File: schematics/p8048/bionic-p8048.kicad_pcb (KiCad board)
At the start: 2 copper layers, 27.9 x 68.6 mm, 9 parts, among them J1 Bionic-P135, J2 Bionic-P245, U1 P8048AH, U2 11AA010-I/TT

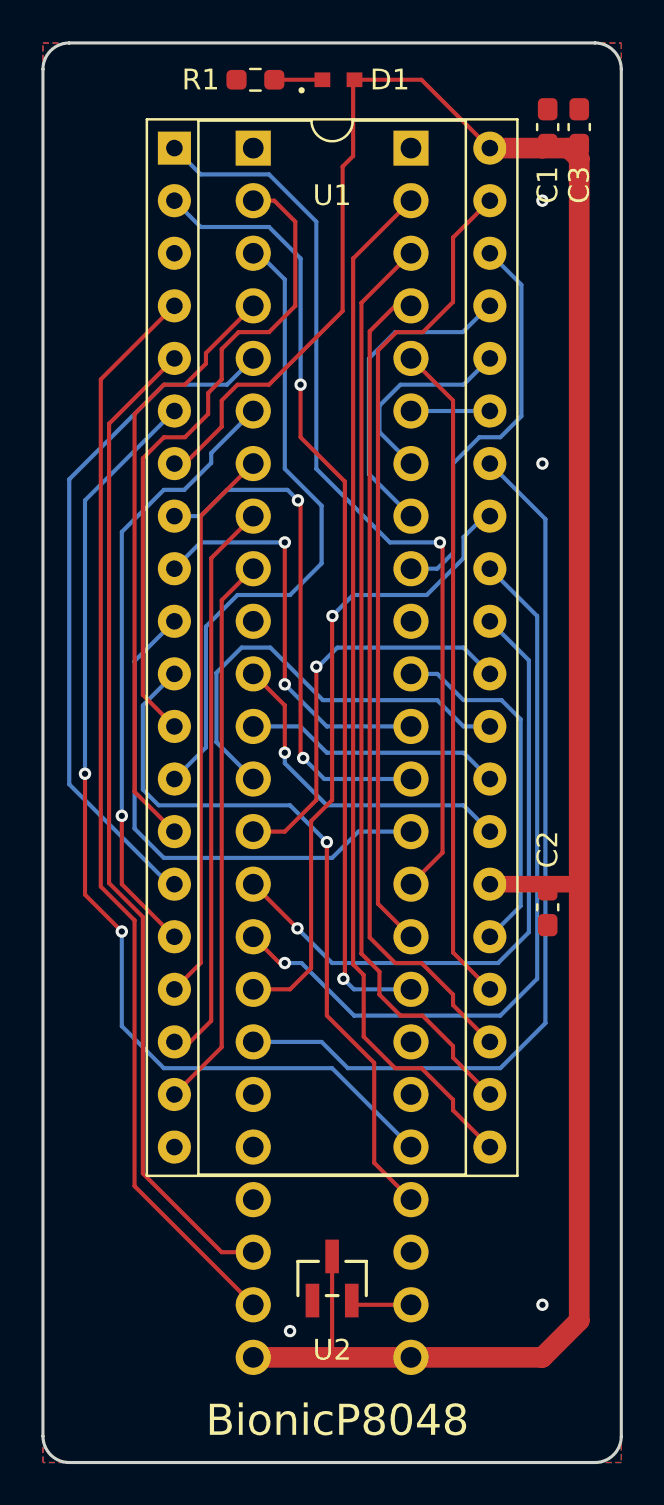
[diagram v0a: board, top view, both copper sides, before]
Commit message: [P8048] Fix EEPROM pinout
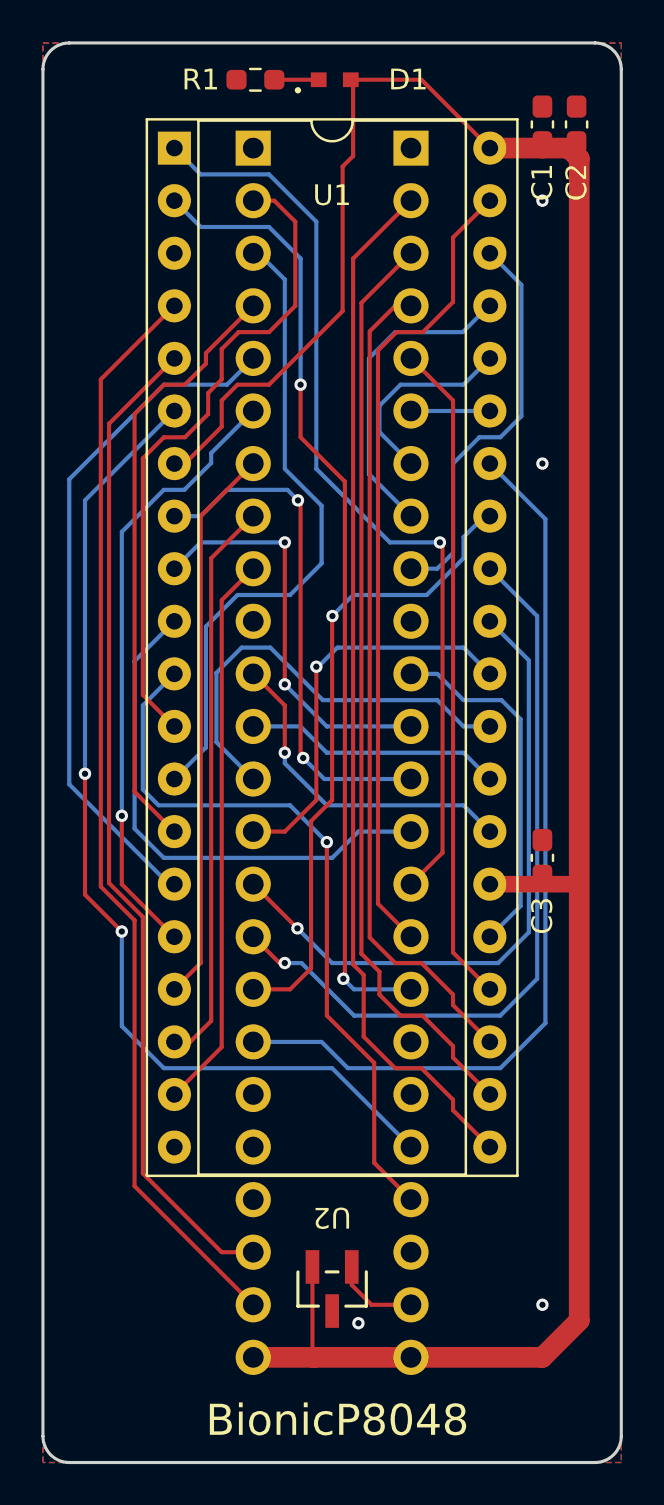
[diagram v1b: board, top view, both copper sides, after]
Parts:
- C2: renamed from C1; value 0.1u -> 22u
- C3: value 22u -> 0.1u
- moved C1 37.8 mm to (125.1, 73.9), turned to 90 degrees
- moved C3 35.4 mm to (125.1, 109.4)
- moved C2 1.40 mm to (126.8, 73.9)
- moved U2 0.51 mm to (115.0, 130.2), turned to 180 degrees
- moved D1 0.18 mm to (115.1, 71.8)
- renumbered C2 to C1
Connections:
- U2 pad 1: GND -> Net-(J2-P57)
- U2 pad 2: Net-(J2-P57) -> VCC
- U2 pad 3: VCC -> GND
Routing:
- net Net-(J2-P57): track 2.94 -> 4.13 mm
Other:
- board text added: "Rev. 5"
- board text removed: "Rev. 4"

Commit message: [P8048] Shrink board size
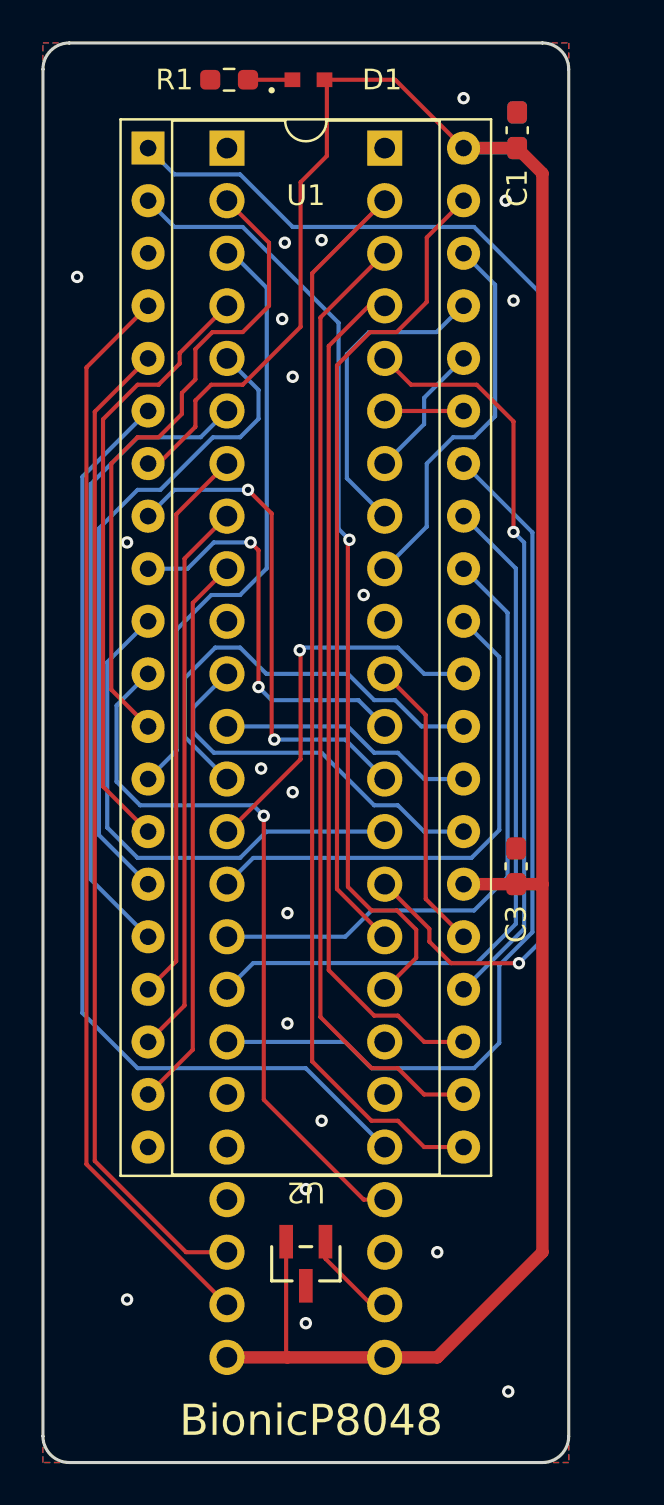
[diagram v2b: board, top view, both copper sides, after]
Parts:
- C2: moved to B.Cu
- moved C2 2.88 mm to (123.9, 74.2)
- moved U2 1.76 mm to (113.7, 129.0)
- moved C3 1.33 mm to (123.9, 109.8)
- moved D1 1.27 mm to (113.8, 71.8)
- moved J1 1.27 mm to (109.9, 75.1)
- moved J2 1.27 mm to (117.5, 75.1)
- moved R1 1.27 mm to (110.0, 71.8)
- moved U1 1.27 mm to (106.1, 75.1)
- moved C1 1.25 mm to (123.9, 74.2)
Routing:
- net /P44: track 44.9 -> 63.1 mm
- net /P34: track 31.3 -> 25.0 mm, vias 1 -> 0
- net /P35: track 36.8 -> 30.5 mm, vias 1 -> 0
- net /P36: track 30.9 -> 36.0 mm, vias 1 -> 0
- net /P23: track 32.1 -> 36.3 mm, vias 0 -> 1
- net /P40: track 17.3 -> 14.3 mm
- net /P25: track 9.71 -> 6.66 mm
- net /P30: track 16.2 -> 18.5 mm, vias 1 -> 0
- net /P21: track 44.8 -> 46.7 mm
- net /P11: track 31.4 -> 29.5 mm
- net /P20: track 50.4 -> 52.1 mm
- net /P22: track 40.0 -> 41.6 mm
- net /P13: track 33.1 -> 31.6 mm
- net /P14: track 29.7 -> 31.1 mm, vias 1 -> 0
- net /P54: track 48.6 -> 47.7 mm, vias 2 -> 0
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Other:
- board size 27.9 x 68.6 mm -> 25.4 x 68.6 mm

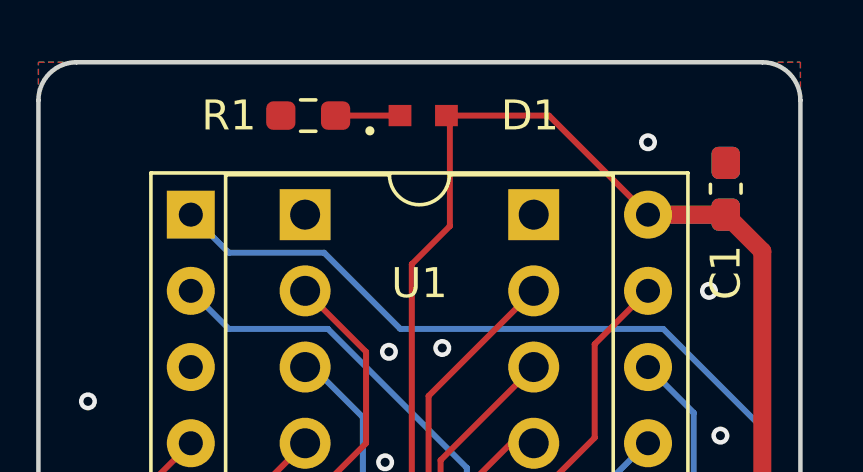
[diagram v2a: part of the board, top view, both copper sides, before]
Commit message: [schematics] Update LED footprint
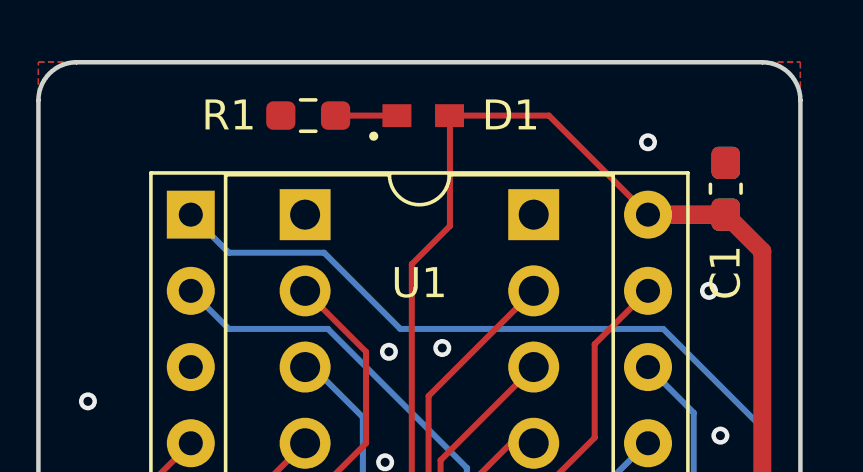
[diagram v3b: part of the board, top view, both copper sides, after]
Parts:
- D1: footprint 0-LocalLibrary:LED_CSL1901UW1_ROM -> 0-LocalLibrary:LED_CSL1901UW1_ROM-M

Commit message: [P8048] Cleanup schematics
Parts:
- D1: footprint 0-LocalLibrary:LED_CSL1901UW1_ROM-M -> rhom:LED_CSL1901UW1_ROM-M
- J1: footprint 0-LocalLibrary:Bionic-P135_Vertical -> bionic:Bionic-P135_Vertical
- J2: footprint 0-LocalLibrary:Bionic-P245_Vertical -> bionic:Bionic-P245_Vertical
- U1: footprint 0-LocalLibrary:DIP-40_W15.24mm_Socket -> bionic:DIP-40_W15.24mm_Socket
- U2: footprint 0-LocalLibrary:SOT-23_MC_MCH-M -> microchip:SOT-23_MC_MCH-M
- moved U2 0.41 mm to (113.7, 129.4)
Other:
- rule pad_to_mask_clearance: 0.051 -> 0

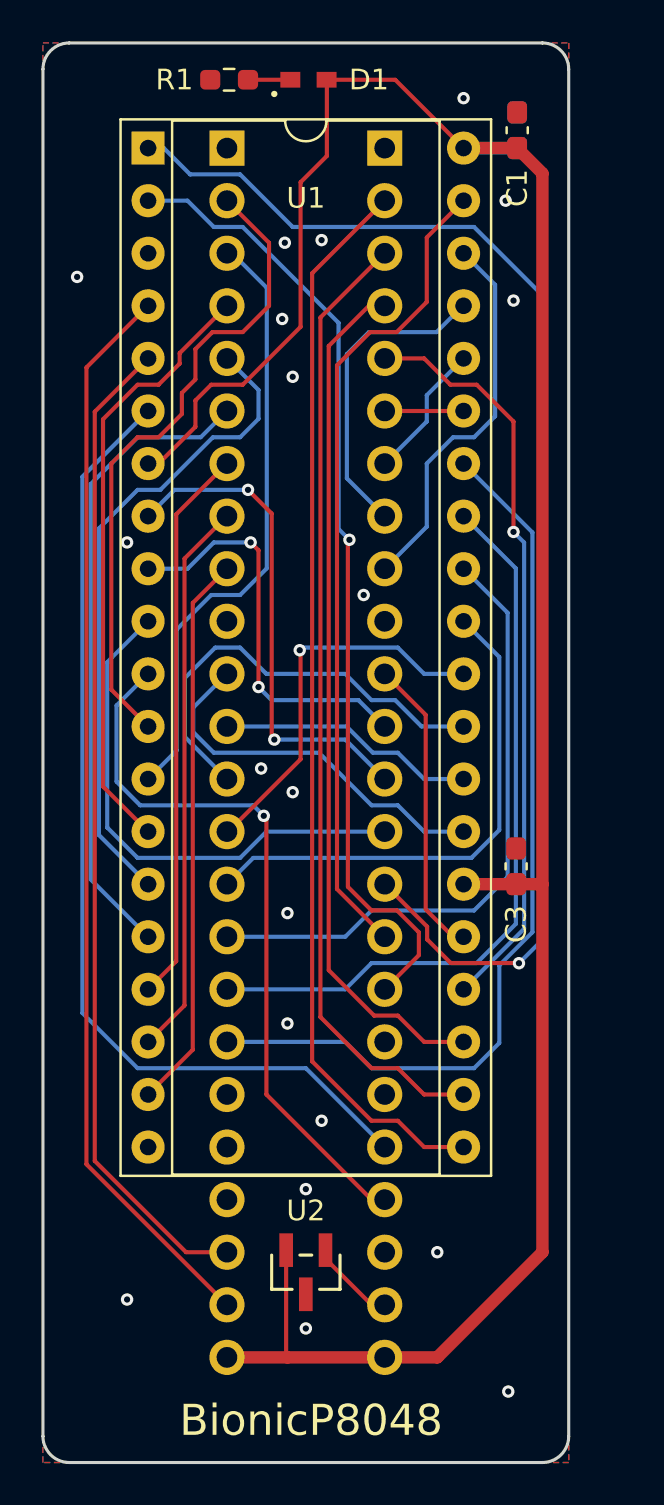
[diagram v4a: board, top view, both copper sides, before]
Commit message: [P8048] Update schematics
Remove unused pins from bionic connector
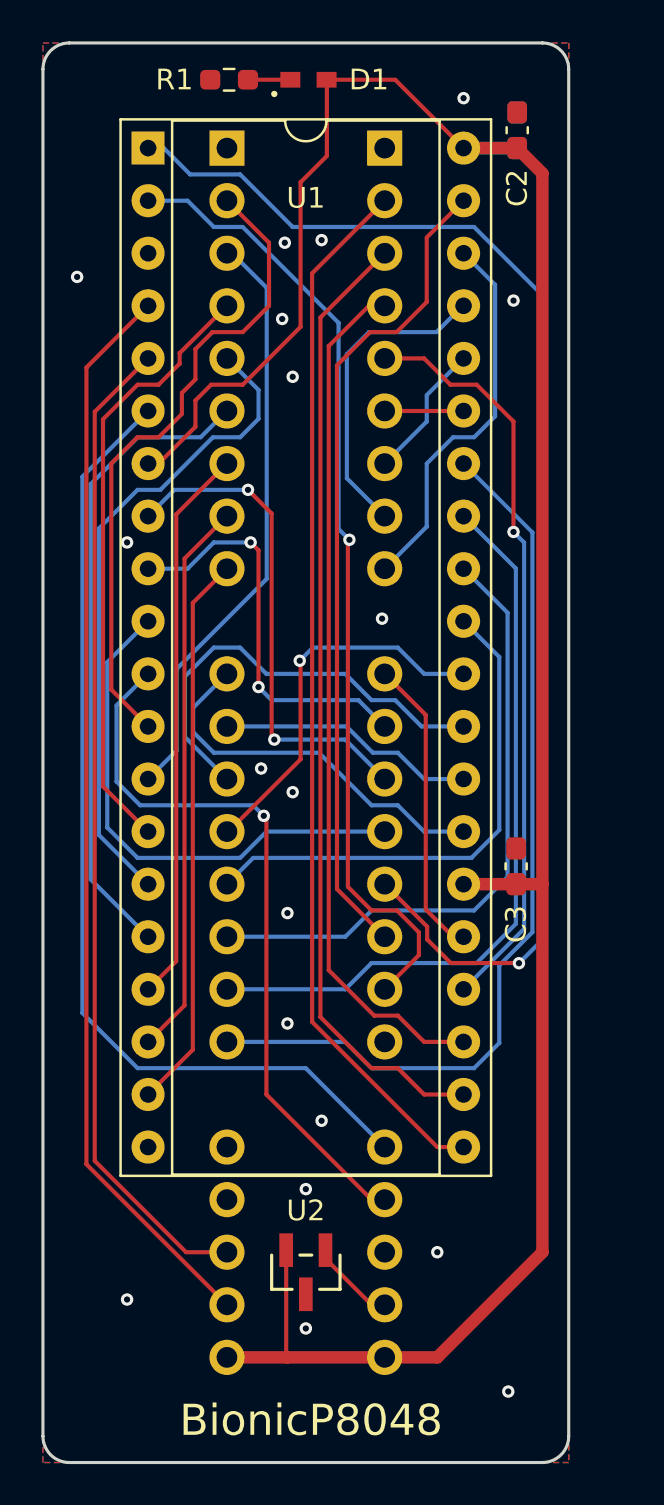
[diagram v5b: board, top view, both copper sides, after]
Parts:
- C1: moved to B.Cu
- C2: moved to F.Cu
- J1: footprint bionic:Bionic-P135_Vertical -> bionic:Bionic-P135_THT
- J2: footprint bionic:Bionic-P245_Vertical -> bionic:Bionic-P245_THT
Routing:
- net /P20: track 52.1 -> 50.9 mm
- net /P11: track 29.5 -> 28.7 mm
- net GND: vias 20 -> 19
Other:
- board text added: "Rev. 6"
- board text removed: "Rev. 5"
